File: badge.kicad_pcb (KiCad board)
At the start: 2 copper layers, 76.2 x 127 mm, 28 parts, among them SW1 SW_Push, SW2 SW_Push, SW3 SW_Push, SW4 SW_Push, SW5 SW_Push, U1 NHD-C12832A1Z-FSRGB-FBW-3V

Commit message: ready for production
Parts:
- renumbered REF** to FTLOGO, REF** to LANYARD
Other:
- board text added: "FurryTel Badge Rev. 1"
- board text removed: "FurryTel Badge Rev. 1 BETA 1"
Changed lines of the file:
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@@
 		(layer "F.Cu")
 		(at 63.323589 27.94)
-		(property "Reference" "REF**"
+		(property "Reference" "LANYARD"
 			(at 0 -0.5 0)
 			(unlocked yes)
@@
 			)
 		)
-		(attr smd)
+		(attr smd board_only)
 		(duplicate_pad_numbers_are_jumpers no)
 		(fp_poly
@@
 		(layer "F.Cu")
 		(at 26.67 144.795188)
-		(property "Reference" "REF**"
+		(property "Reference" "FTLOGO"
 			(at 0 -0.5 0)
 			(unlocked yes)
@@
 			)
 		)
-		(attr smd exclude_from_bom)
+		(attr smd board_only exclude_from_bom)
 		(duplicate_pad_numbers_are_jumpers no)
 		(fp_poly
@@
 		(sheetname "/")
 		(sheetfile "badge.kicad_sch")
-		(units
-			(unit
-				(name "A")
-				(pins "30" "37" "1" "2" "4" "5" "6" "7" "9" "10" "11" "12" "14" "15"
-					"16" "17" "19" "20" "39" "40" "18" "23" "28" "13" "8" "38" "3" "36"
-					"21" "22" "24" "25" "26" "27" "29" "35" "31" "32" "34" "33"
-				)
-			)
-		)
 		(attr smd)
 		(duplicate_pad_numbers_are_jumpers no)
@@
 		)
 		(group ""
-			(members "182fb076-7a73-40a9-8792-f3c44c90d906" "30480dfc-4ed9-4b33-bbbd-7ee2dbf10ede")
-		)
-		(group ""
 			(members "0411d33e-77aa-45e4-8a90-5b5e99fb055f" "099de2bf-8369-4fc1-a133-8458c0eb42c2"
 				"0a103adc-9088-4843-8afb-7e433f041f15" "0c4934ce-17d6-4436-be9a-570a53d4988a"
@@
 		)
 		(group ""
+			(members "182fb076-7a73-40a9-8792-f3c44c90d906" "30480dfc-4ed9-4b33-bbbd-7ee2dbf10ede")
+		)
+		(group ""
 			(members "13aeea67-bd4d-4c6f-8816-98b7827a5a30" "13d995c2-1e2e-407f-aba3-cc990d59728f"
 				"1ce28c5e-9c23-4722-9d14-917e33b50658" "73289d76-fb04-4452-ac8b-c9b60a1dacd4"
@@
 		(layer "Edge.Cuts")
 	)
-	(gr_text "FurryTel Badge\nRev. 1 BETA 1"
+	(gr_text "FurryTel Badge\nRev. 1"
 		(at 34.044783 149.571524 0)
 		(layer "F.SilkS")

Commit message: pawsgit push
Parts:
- added J1: TC2030, FTbadge:Paw-Connect_RevB_TC2030-IDC-NL_2x03_P1.27mm_Vertical, F.Cu at (97.0, 148.9)
- A1: footprint Module:RaspberryPi_Pico_Common_SMD -> Module:RaspberryPi_Pico_SMD_HandSolder
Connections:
- A1 pad 30: unconnected-(A1-RUN-Pad30) -> Net-(A1-RUN)
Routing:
- net Net-(A1-RUN): track 0.00 -> 174.2 mm
- net Net-(A1-SWDIO): track 0.00 -> 112.0 mm, vias 0 -> 3
- net Net-(A1-SWCLK): track 0.00 -> 109.7 mm, vias 0 -> 2
- net GND: track 110.0 -> 120.1 mm, vias 24 -> 25
- net Net-(A1-GPIO4): track 74.9 -> 76.3 mm

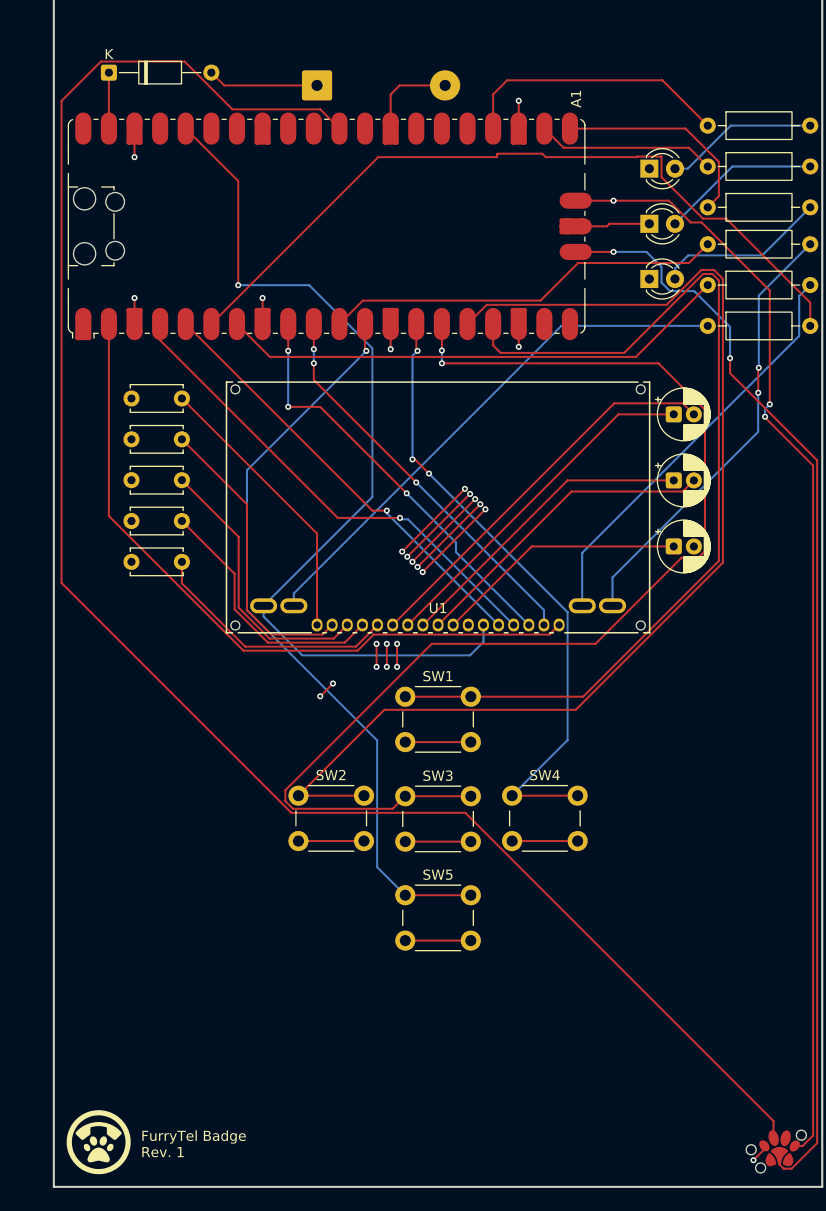
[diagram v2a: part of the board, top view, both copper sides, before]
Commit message: nudge some vias and traces and capacitors around, more via stitching
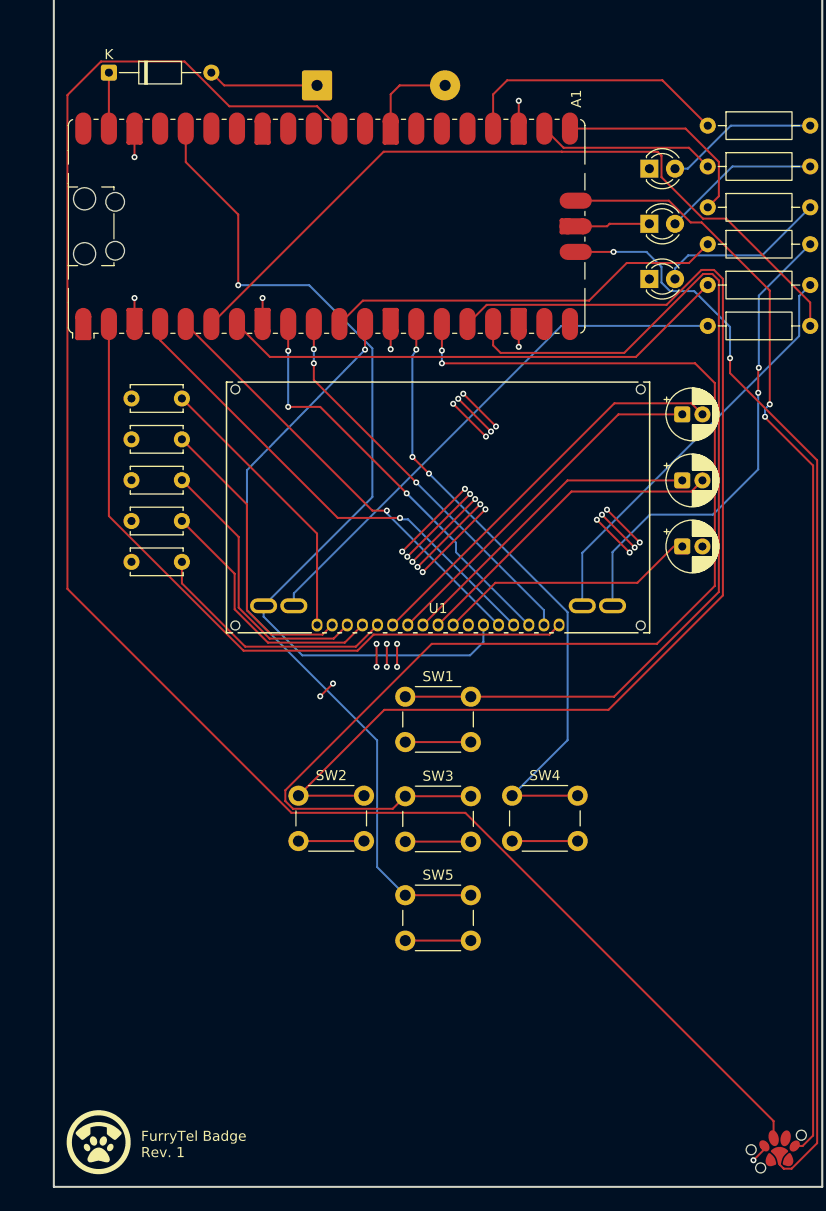
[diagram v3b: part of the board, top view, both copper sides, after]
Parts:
- moved C6 0.85 mm to (87.7, 75.8)
- moved C7 0.85 mm to (87.7, 82.3)
- moved C8 0.85 mm to (87.7, 88.9)
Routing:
- net GND: track 120.1 -> 147.3 mm, vias 25 -> 37
- net Net-(A1-GPIO11): track 117.6 -> 123.2 mm
- net Net-(U1-(B)LED-): track 44.0 -> 47.6 mm
- net Net-(A1-GPIO12): track 114.2 -> 116.1 mm
- net Net-(A1-GPIO13): track 92.8 -> 94.6 mm
- net Net-(U1-C2-): track 39.4 -> 40.3 mm
- net Net-(U1-C1-): track 31.3 -> 32.2 mm
- net Net-(A1-SWDIO): vias 3 -> 2
